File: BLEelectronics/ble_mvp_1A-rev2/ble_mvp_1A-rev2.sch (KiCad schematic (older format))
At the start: 19 parts, among them IC1 LTC4412xS6, IC2 PCF8523T, IC3 MX25R6435FM2IL0, J1 Nordic_nRF52840_breakout, Q1 Si2307CDS, U1 BAT-HLD-001, U4 LP5907MFX-3.3, X1 32.768KHZ

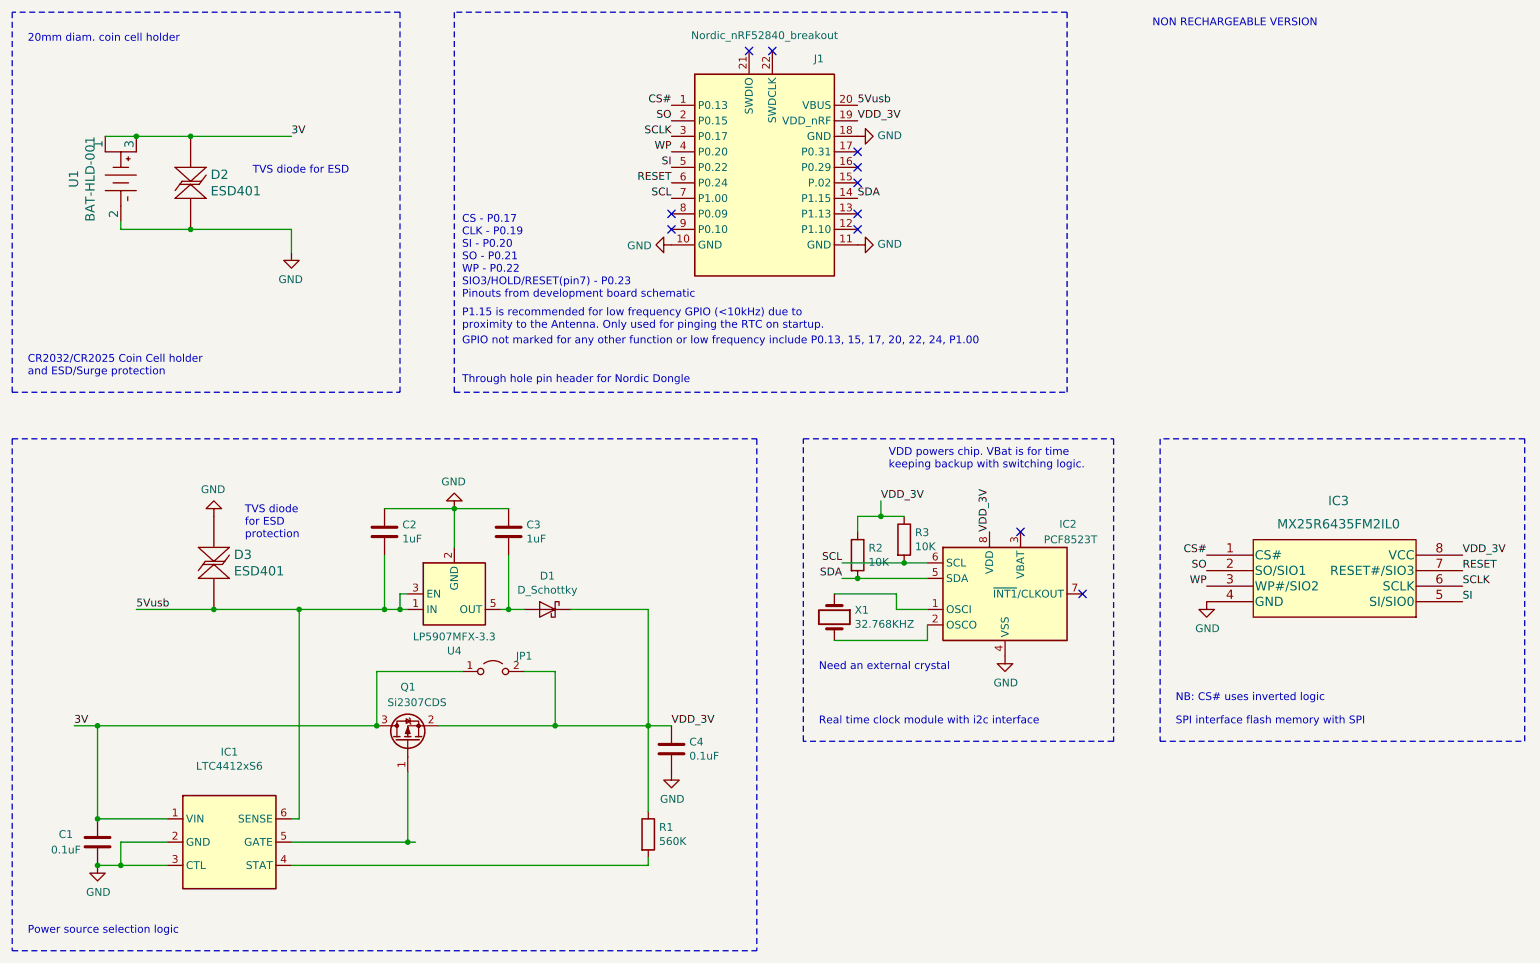
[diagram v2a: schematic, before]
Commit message: Additional changes to schematic labelling.
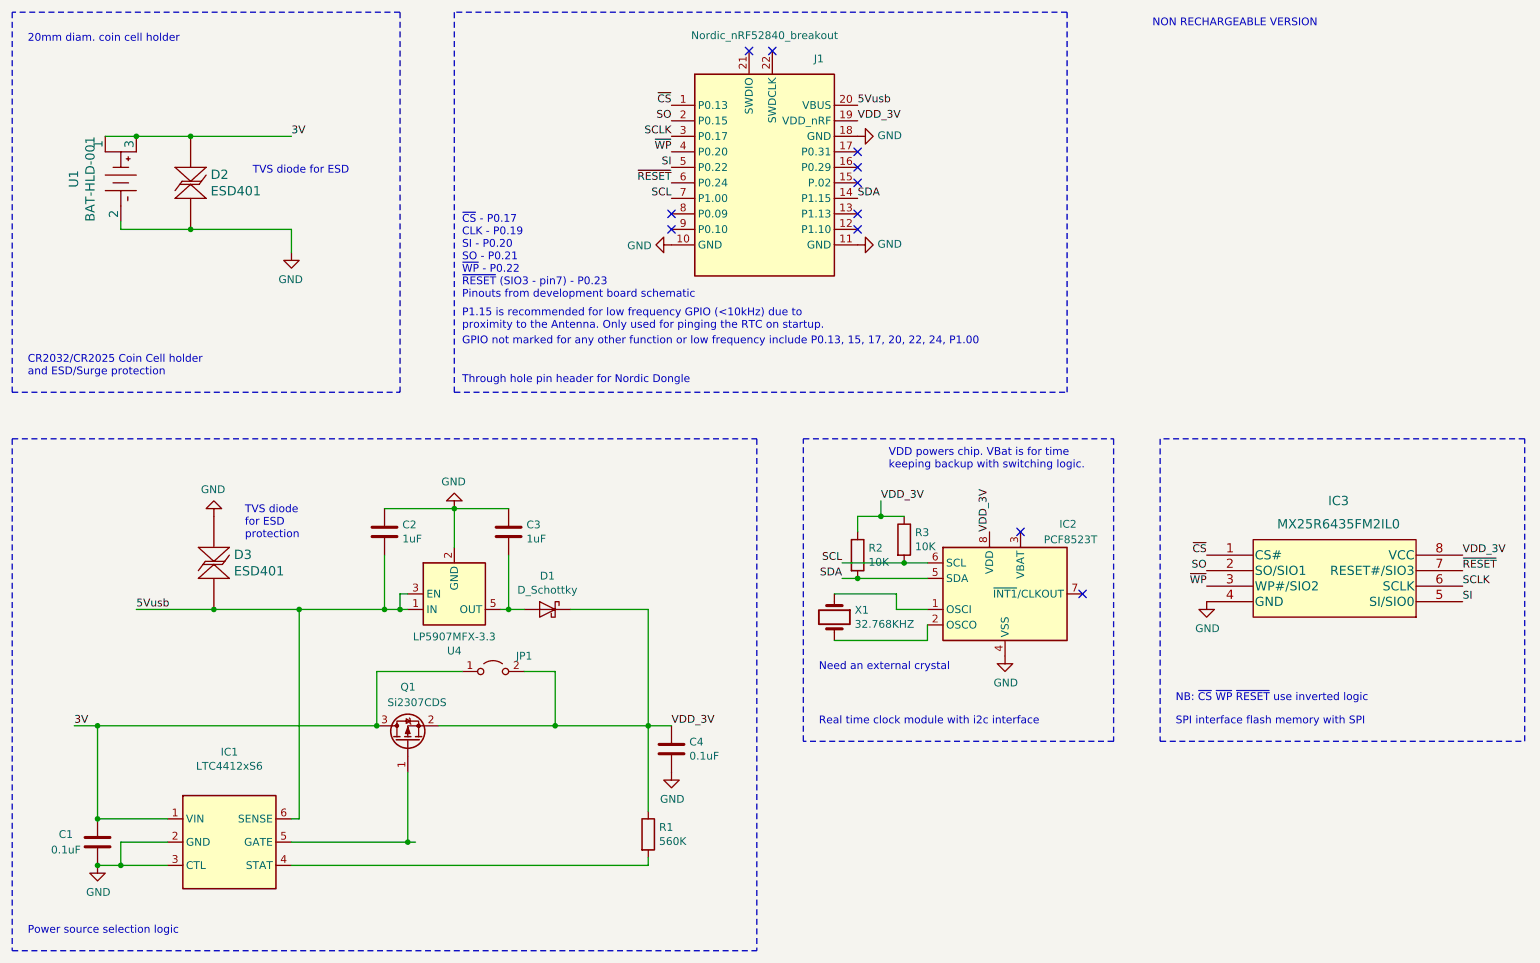
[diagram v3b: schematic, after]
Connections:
- net CS# renamed ~CS~
- net RESET renamed ~RESET~
- net WP renamed ~WP~
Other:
- note added: "NB: ~CS~ ~WP~ ~RESET~ use inverted logic"
- note added: "~CS~ - P0.17\nCLK - P0.19\nSI - P0.20\nSO - P0.21\n~WP~ - P0.22\n~RESET~ (SIO3 - pin7) - P0.23\nPinouts from development board schematic\n"
- note removed: "CS - P0.17\nCLK - P0.19\nSI - P0.20\nSO - P0.21\nWP - P0.22\nSIO3/HOLD/RESET(pin7) - P0.23\nPinouts from development board schematic\n"
- note removed: "NB: CS# uses inverted logic"
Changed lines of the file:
@@
 SO
 Text Label 10400 4500 0    50   ~ 0
-RESET
+~RESET~
 Text Label 8750 4400 2    50   ~ 0
-CS#
+~CS~
 Text Label 5300 1600 2    50   ~ 0
 SO
 Text Label 5300 1500 2    50   ~ 0
-CS#
+~CS~
 Text Label 5300 1900 2    50   ~ 0
 SI
@@
 P1.15 is recommended for low frequency GPIO (<10kHz) due to\nproximity to the Antenna. Only used for pinging the RTC on startup.
 Text Label 5300 1800 2    50   ~ 0
-WP
+~WP~
 Text Label 8750 4600 2    50   ~ 0
-WP
+~WP~
 Text Label 6650 4050 0    50   ~ 0
 VDD_3V
@@
 TVS diode \nfor ESD\nprotection
 Text Label 5300 2000 2    50   ~ 0
-RESET
+~RESET~
 Text Notes 3950 2750 0    50   ~ 0
-CS - P0.17\nCLK - P0.19\nSI - P0.20\nSO - P0.21\nWP - P0.22\nSIO3/HOLD/RESET(pin7) - P0.23\nPinouts from development board schematic\n
+~CS~ - P0.17\nCLK - P0.19\nSI - P0.20\nSO - P0.21\n~WP~ - P0.22\n~RESET~ (SIO3 - pin7) - P0.23\nPinouts from development board schematic\n
 Text Notes 6700 3850 0    50   ~ 0
 VDD powers chip. VBat is for time \nkeeping backup with switching logic.
@@
 	4550 5500 5150 5500
 Text Notes 8550 5350 0    50   ~ 0
-NB: CS# uses inverted logic
+NB: ~CS~ ~WP~ ~RESET~ use inverted logic
 $EndSCHEMATC
